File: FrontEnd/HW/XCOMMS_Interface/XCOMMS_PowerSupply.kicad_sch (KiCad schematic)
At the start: 75 parts

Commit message: Altium to KiCad translation of interface board
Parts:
- removed C? (x3): Cap Semi, 0603 SMD Capacitor, symbol PowerSupply-altium-import:2_Cap Semi
- removed C? (x6): Cap Semi, 0805 SMD Capacitor, symbol PowerSupply-altium-import:3_mirrored_Cap Semi
- removed C? (x6): Cap Semi, 0805 SMD Capacitor, symbol PowerSupply-altium-import:0_mirrored_Cap Semi
- removed C? (x11): Cap Semi, 0603 SMD Capacitor, symbol PowerSupply-altium-import:3_mirrored_Cap Semi
- removed C? (x3): Cap Semi, 0603 SMD Capacitor, symbol PowerSupply-altium-import:0_mirrored_Cap Semi
- removed C? (x3): Cap Semi, 0603 SMD Capacitor, symbol PowerSupply-altium-import:2_mirrored_Cap Semi
- removed C?: Cap Semi, 0603 SMD Capacitor, symbol PowerSupply-altium-import:3_Cap Semi
- removed C?: Cap Semi, 0603 SMD Capacitor, symbol PowerSupply-altium-import:1_mirrored_Cap Semi
- removed L? (x2): 652-SRP5030T-3R3M, Bourns_SRP5030T-3R3M, symbol PowerSupply-altium-import:0_Inductor
- removed L?: WE_74438356022, Coilcraft_XAL60xx, symbol PowerSupply-altium-import:0_Inductor
- removed R? (x9): Res3, 0603 SMD Resistor, symbol PowerSupply-altium-import:1_Res3
- removed R? (x4): Res3, 0603 SMD Resistor, symbol PowerSupply-altium-import:0_Res3
- removed R? (x7): Res3, 0603 SMD Resistor, symbol PowerSupply-altium-import:3_Res3
- removed Rsense? (x2): Res3, 1206 SMD RESISTOR, symbol PowerSupply-altium-import:0_Res3
- removed TP? (x6): TP, TestPoint, symbol PowerSupply-altium-import:3_TP_d1.5mm
- removed TP?: TP, TestPoint, symbol PowerSupply-altium-import:1_TP_d1.5mm
- removed U? (x2): MAX870EUK, SOT23-5N, symbol PowerSupply-altium-import:0_MAX870EUK
- removed U? (x3): TPS56637RPAR, CONV_TPS56637RPAR, symbol PowerSupply-altium-import:0_TPS56637RPAR
- added C10, C11, C13, C14, C19, C20, C21, C22, C23, C24, C7, C8: 10uF, Capacitor_SMD:C_0805_2012Metric, symbol Device:C
- added C12, C15, C16, C17, C18, C28, C9: 100nF, Capacitor_SMD:C_0603_1608Metric, symbol Device:C
- added C25, C26, C27: 100pF, Capacitor_SMD:C_0603_1608Metric, symbol Device:C
- added C29, C33, C34, C35, C36, C37, C38, C39, C40: 0.33uF, Capacitor_SMD:C_0603_1608Metric, symbol Device:C
- added C30, C31, C32: 1uF, Capacitor_SMD:C_0603_1608Metric, symbol Device:C
- added L1, L2: 3.3uH, Inductor_SMD:L_Bourns_SRP5030T, symbol Device:L
- added L3: 2.2uH, Inductor_SMD:L_Coilcraft_XAL60xx_6.36x6.56mm, symbol Device:L
- added R10, R11, R12, R13, R16, R20: 10k, Resistor_SMD:R_0603_1608Metric, symbol Device:R
- added R14: 0R, Resistor_SMD:R_0603_1608Metric, symbol Device:R
- added R15, R17, R18, R21, R4, R6, R8: 20k, Resistor_SMD:R_0603_1608Metric, symbol Device:R
- added R19: 5k, Resistor_SMD:R_0603_1608Metric, symbol Device:R
- added R2: 169k, Resistor_SMD:R_0603_1608Metric, symbol Device:R
- added R3: 90.9k, Resistor_SMD:R_0603_1608Metric, symbol Device:R
- added R5: 73.2k, Resistor_SMD:R_0603_1608Metric, symbol Device:R
- added R7: 45.3k, Resistor_SMD:R_0603_1608Metric, symbol Device:R
- added R9: 36.1k, Resistor_SMD:R_0603_1608Metric, symbol Device:R
- added Rsense1, Rsense2: 0R005, Resistor_SMD:R_1206_3216Metric, symbol Device:R
- added TP1, TP2, TP3, TP4, TP5, TP6, TP7: TestPoint, TestPoint:TestPoint_Pad_D1.0mm, symbol Connector:TestPoint
- added U10, U9: MAX870EUK, Package_TO_SOT_SMD:SOT-23-5, symbol GGS_Power:MAX870
- added U2, U3, U4: TPS56637, GGS_Power:TPS56637RPAR, symbol GGS_Power:TPS56637
- U5: renamed from U?; footprint SOT23-5N -> Package_TO_SOT_SMD:SOT-23-5; symbol PowerSupply-altium-import:0_TPS784 -> GGS_Power:TPS784
- U6: renamed from U?; footprint SOT23-5N -> Package_TO_SOT_SMD:SOT-23-5; symbol PowerSupply-altium-import:0_MAX870EUK -> GGS_Power:MAX870
- U7: renamed from U?; footprint SC70-5 -> GGS_Miscellaneous:SC70-5; symbol PowerSupply-altium-import:3_INA290 -> GGS_Miscellaneous:INA290
- U8: renamed from U?; footprint SOT-28-8N -> Package_TO_SOT_SMD:SOT-23-8; symbol PowerSupply-altium-import:0_AD5160 -> GGS_Miscellaneous:AD1560
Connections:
- net 5V_EN: now also U3.1 (EN)
- net 6V: now also C19.1, C22.1, L1.2, R3.1, R4.1, Rsense1.1, Rsense2.1, TP1.1
- net 6V_EN: now also U2.1 (EN)
- net GND: now also C10.2, C11.2, C12.2, C13.2, C14.2, C15.2, C19.2, C20.2, C21.2, C22.2, C23.2, C24.2, C28.1, C29.1, C30.2, C31.2, C32.2, C33.1, C35.1, C36.1, C38.1, C39.1, C7.2, C8.2, C9.2, R10.2, R11.2, R12.2, R15.2, R17.2, R19.2, R21.2, R9.2, U10.4 (GND), U2.10 (MODE), U2.3 (AGND), U2.9 (PGND), U3.10 (MODE), U3.3 (AGND), U3.9 (PGND), U4.10 (MODE), U4.3 (AGND), U4.9 (PGND), U9.4 (GND)
- net Vd_PA: now also Rsense1.2, Rsense2.2
- net Vg_PA1: now also R13.2, R15.1, TP4.1
- net Vg_PA2: now also R16.2, R17.1, TP6.1
- net Vg_PA3: now also R20.2, R21.1, TP7.1
- net Vinv_in: now also C33.2, C36.2, C39.2, R14.2, U10.2 (IN), U9.2 (IN)
- net at U5.4 (FB), U8.7 (B): now also R18.1
- net at U5.5 (OUT), U8.1 (W): now also C31.1, C32.1, R14.1, TP5.1
- net at U6.1 (OUT): now also C29.2, R13.1
- net at U6.5 (C1+): now also C34.2
- net at U6.3 (C1-): now also C34.1
- net 3V3 renamed +3V3
- net +3V3: now also C21.1, C24.1, C30.1, L3.2, R7.1, R8.1, TP3.1; no longer U8.2 (VDD)
- net 5V renamed +5V
- net +5V: now also C20.1, C23.1, C28.2, L2.2, R5.1, R6.1, TP2.1
- new net: C17.1, U3.7 (BOOT)
- new net: C17.2, L2.1, U3.6 (SW)
- new net: C27.2, R8.2
- new net: C26.1, R11.1, R5.2, U3.2 (FB)
- new net: C18.1, U4.7 (BOOT)
- new net: C18.2, L3.1, U4.6 (SW)
- new net: R18.2, R19.1
- new net: C38.2, R20.1, U10.1 (OUT)
- new net: C16.1, U2.7 (BOOT)
- new net: C16.2, L1.1, U2.6 (SW)
- new net: C27.1, R12.1, R7.2, U4.2 (FB)
- new net: R2.2, R9.1, U4.1 (EN)
- new net: C25.1, R10.1, R3.2, U2.2 (FB)
- new net: C40.1, U10.3 (C1-)
- new net: C40.2, U10.5 (C1+)
- new net: C25.2, R4.2
- new net: C35.2, R16.1, U9.1 (OUT)
- new net: C26.2, R6.2
- new net: C37.1, U9.3 (C1-)
- new net: C37.2, U9.5 (C1+)
- new net +12V: C10.1, C11.1, C12.1, C13.1, C14.1, C15.1, C7.1, C8.1, C9.1, R2.1, U2.8 (VIN), U3.8 (VIN), U4.8 (VIN)
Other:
- note added: "12 V to 3.3 V Buck-Converter"
- note added: "12 V to 5 V Buck-Converter"
- note added: "12 V to 6 V Buck-Converter"
- note added: "Gate Voltage Regulation"
- note added: "PA Drain Current Sense Amplifier"
- note added: "PA Gate Voltage Inverters"
- note added: "PowerSupply File Outputs"
- moved on the sheet: U5, U6

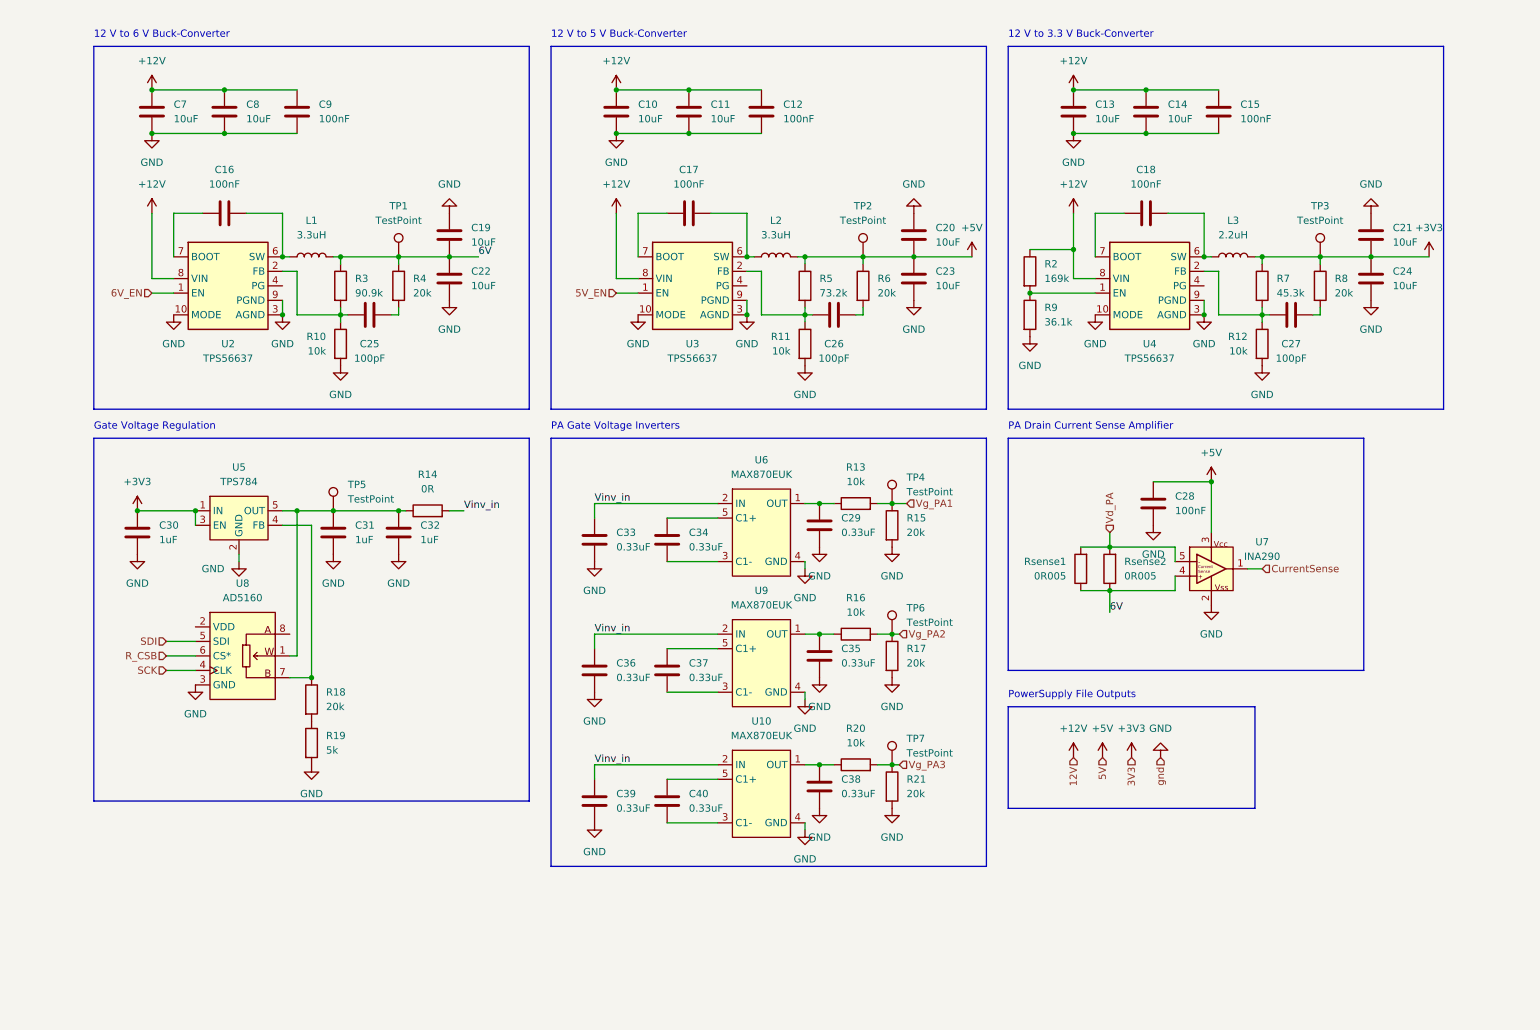
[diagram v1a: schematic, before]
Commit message: XCOMMS_RF and XCOMMS_Interface KiCad design updated
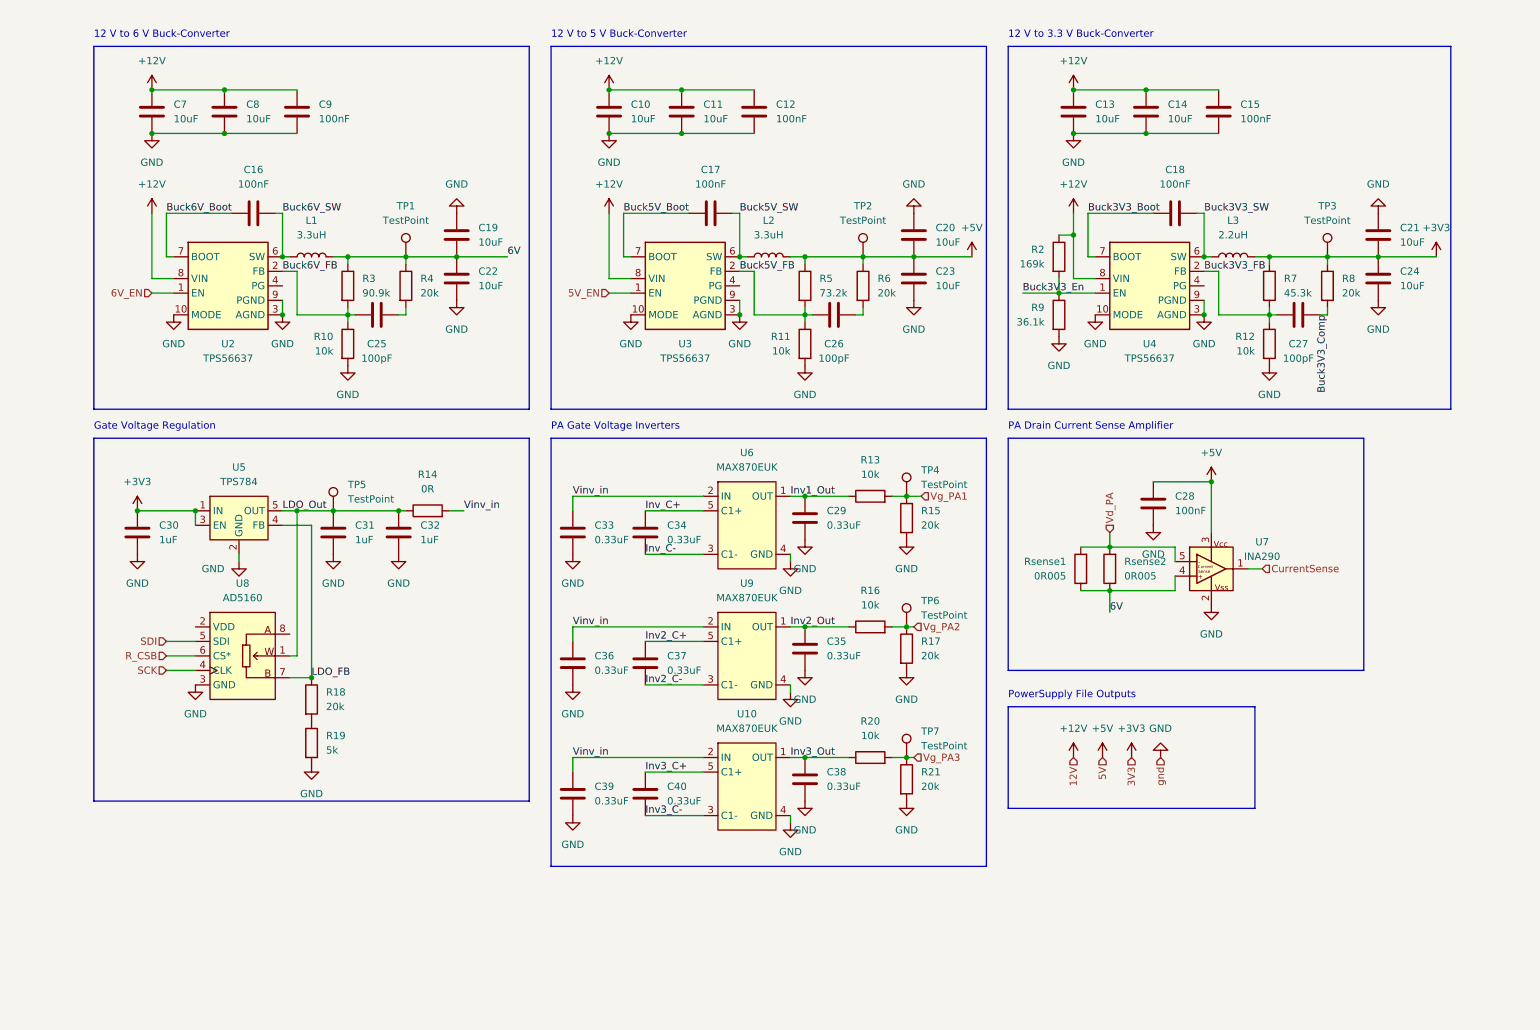
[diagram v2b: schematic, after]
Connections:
- net Buck5V_Boot: now reaches C17.1, U3.7 (BOOT)
- net Buck5V_SW: now reaches C17.2, L2.1, U3.6 (SW)
- net Inv1_Out: now reaches C29.2, R13.1, U6.1 (OUT)
- net Buck3V3_Comp: now reaches C27.2, R8.2
- net Buck5V_FB: now reaches C26.1, R11.1, R5.2, U3.2 (FB)
- net Buck3V3_Boot: now reaches C18.1, U4.7 (BOOT)
- net Buck3V3_SW: now reaches C18.2, L3.1, U4.6 (SW)
- net LDO_FB: now reaches R18.1, U5.4 (FB), U8.7 (B)
- net Inv3_Out: now reaches C38.2, R20.1, U10.1 (OUT)
- net LDO_Out: now reaches C31.1, C32.1, R14.1, TP5.1, U5.5 (OUT), U8.1 (W)
- net Buck6V_Boot: now reaches C16.1, U2.7 (BOOT)
- net Buck6V_SW: now reaches C16.2, L1.1, U2.6 (SW)
- net Buck3V3_FB: now reaches C27.1, R12.1, R7.2, U4.2 (FB)
- net Buck3V3_En: now reaches R2.2, R9.1, U4.1 (EN)
- net Buck6V_FB: now reaches C25.1, R10.1, R3.2, U2.2 (FB)
- net Inv3_C-: now reaches C40.1, U10.3 (C1-)
- net Inv3_C+: now reaches C40.2, U10.5 (C1+)
- net Inv2_Out: now reaches C35.2, R16.1, U9.1 (OUT)
- net Inv2_C-: now reaches C37.1, U9.3 (C1-)
- net Inv2_C+: now reaches C37.2, U9.5 (C1+)
- net Inv_C-: now reaches C34.1, U6.3 (C1-)
- net Inv_C+: now reaches C34.2, U6.5 (C1+)
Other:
- moved on the sheet: C10, C11, C12, C16, C17, C18, C19, C21, C22, C24, C25, C27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

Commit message: XCOMMS Interface rebuild
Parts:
- C10, C11, C13, C14, C19, C20, C21, C22, C23, C24, C7, C8: footprint Capacitor_SMD:C_0805_2012Metric -> Capacitor_SMD:C_0603_1608Metric
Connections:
- net CurrentSense renamed Id_PA
- no-connect marks 0 -> 5
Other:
- note removed: "PowerSupply File Outputs"
- moved on the sheet: C10, C11, C12, C13, C14, C15, C16, C17, C18, C19, C20, C21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

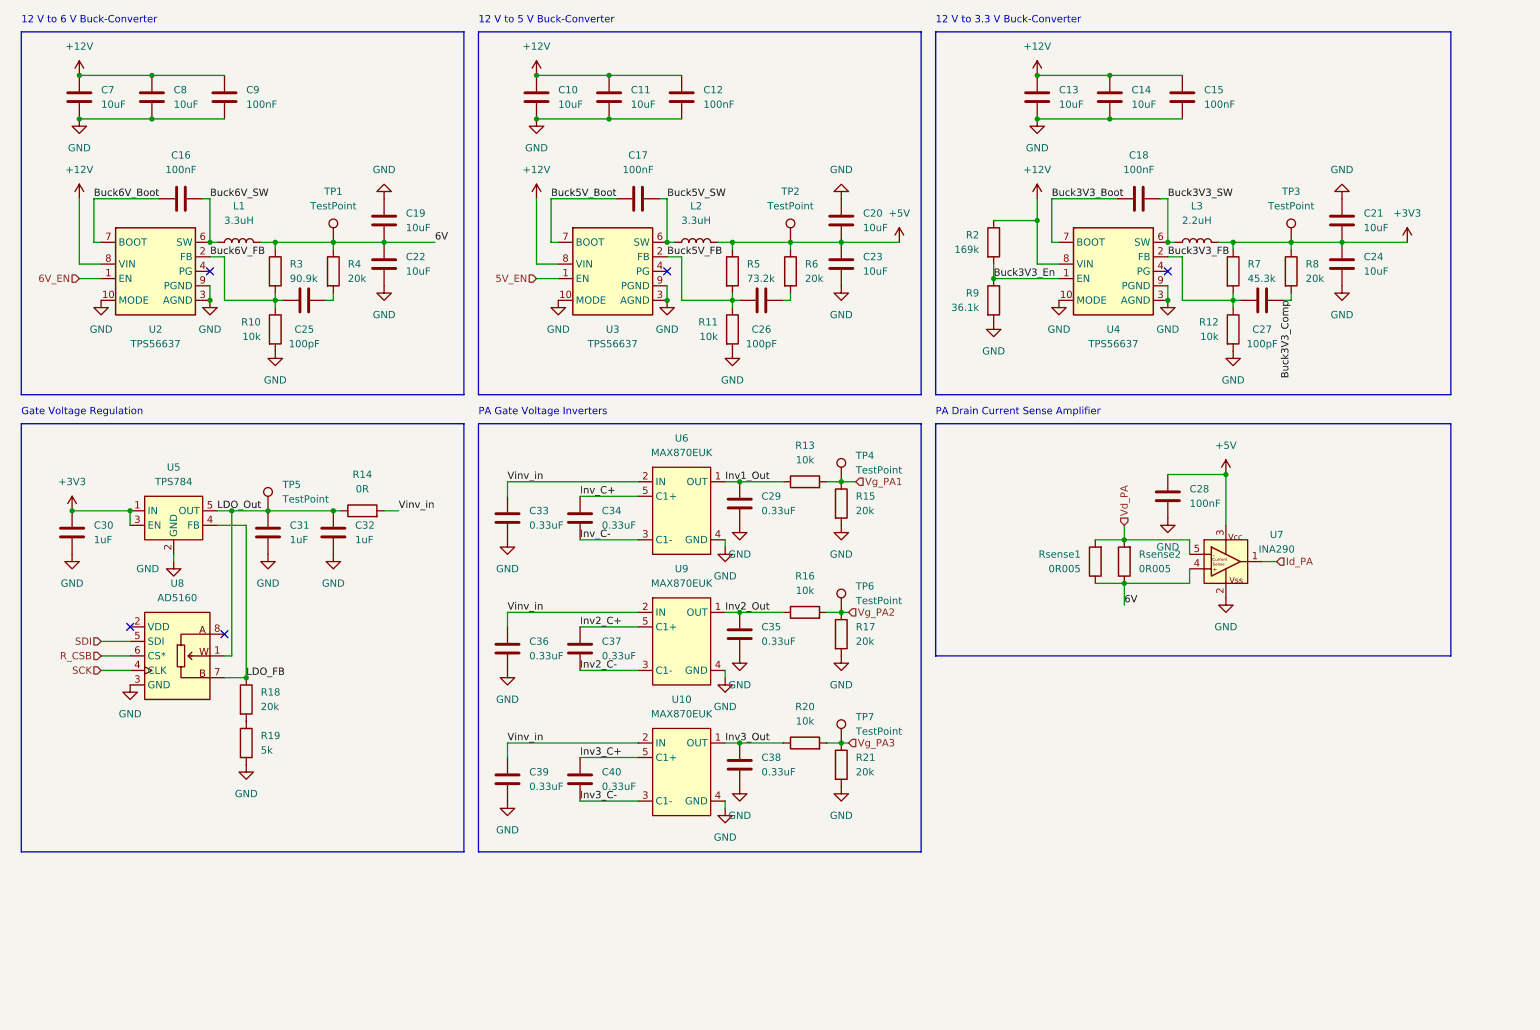
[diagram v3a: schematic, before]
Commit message: simplified PA gate control
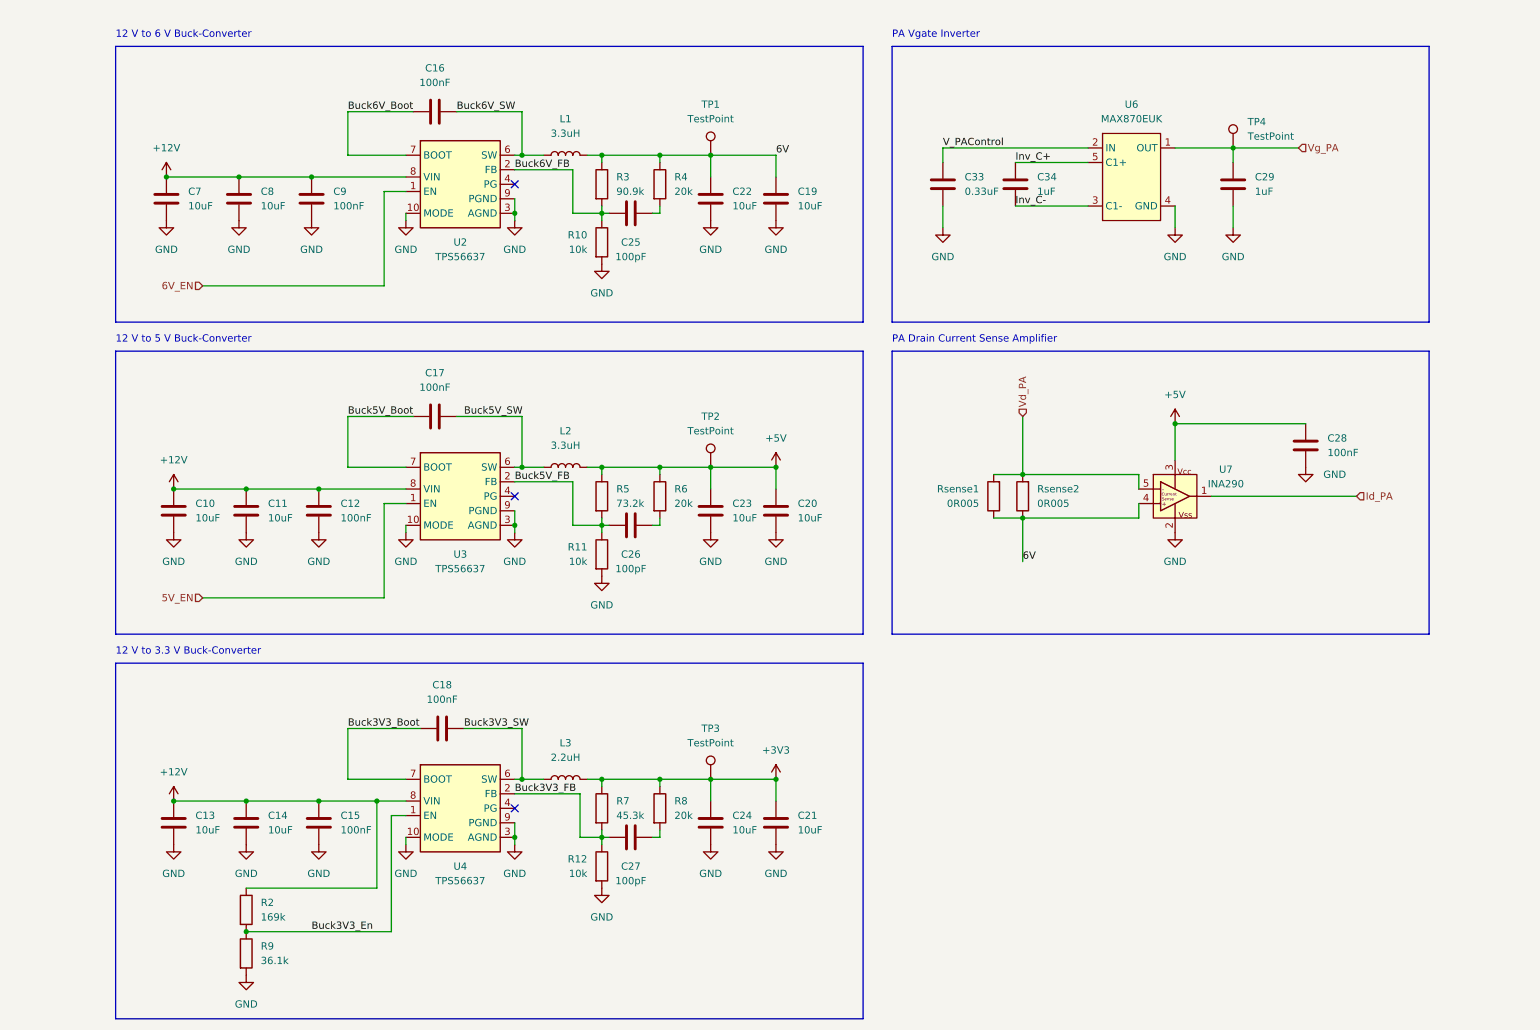
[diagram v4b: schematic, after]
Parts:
- removed C30, C31, C32: 1uF, Capacitor_SMD:C_0603_1608Metric, symbol Device:C
- removed C35, C36, C37, C38, C39, C40: 0.33uF, Capacitor_SMD:C_0603_1608Metric, symbol Device:C
- removed R13, R16, R20: 10k, Resistor_SMD:R_0603_1608Metric, symbol Device:R
- removed R14: 0R, Resistor_SMD:R_0603_1608Metric, symbol Device:R
- removed R15, R17, R18, R21: 20k, Resistor_SMD:R_0603_1608Metric, symbol Device:R
- removed R19: 5k, Resistor_SMD:R_0603_1608Metric, symbol Device:R
- removed TP5, TP6, TP7: TestPoint, TestPoint:TestPoint_Pad_D1.0mm, symbol Connector:TestPoint
- removed U10, U9: MAX870EUK, Package_TO_SOT_SMD:SOT-23-5, symbol GGS_Power:MAX870
- removed U5: TPS784, Package_TO_SOT_SMD:SOT-23-5, symbol GGS_Power:TPS784
- removed U8: AD5160, Package_TO_SOT_SMD:SOT-23-8, symbol GGS_Miscellaneous:AD1560
- C29, C34: value 0.33uF -> 1uF
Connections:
- net Vg_PA1 is gone; now on net Vg_PA: TP4.1
- net Buck3V3_Comp: no longer names the net of C27.2, R8.2
- net Inv1_Out renamed Vg_PA
- net Vinv_in renamed V_PAControl
- no-connect marks 5 -> 3
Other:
- note added: "PA Vgate Inverter"
- note removed: "Gate Voltage Regulation"
- note removed: "PA Gate Voltage Inverters"
- moved on the sheet: C10, C11, C12, C13, C14, C15, C16, C17, C18, C19, C20, C21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
